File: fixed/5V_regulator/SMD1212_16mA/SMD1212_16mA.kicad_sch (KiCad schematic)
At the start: 14 parts, among them J1 Conn_01x04, J2 Conn_01x04, Q1 MMBT5551L, U1 TPS61222DCK, U2 LMV321

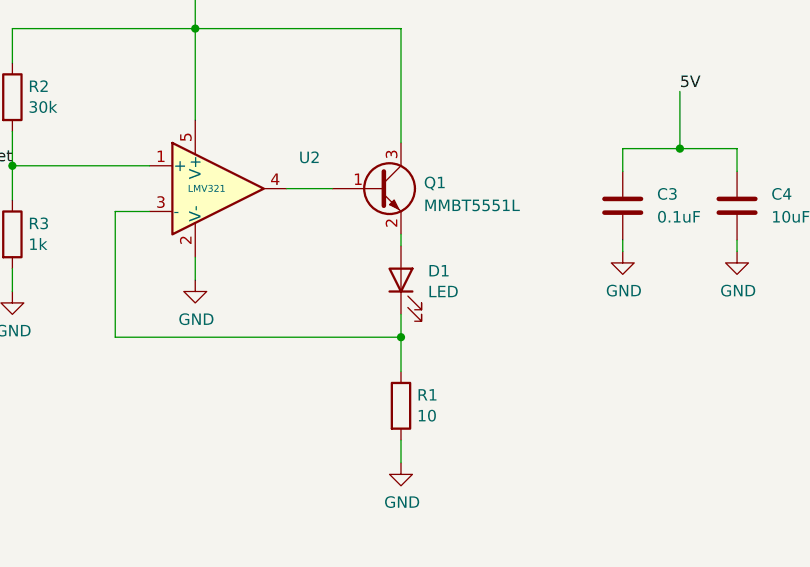
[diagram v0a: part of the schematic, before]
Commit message: Added part # to 'Symbol Fields Table" for SMD1212_16mA design.
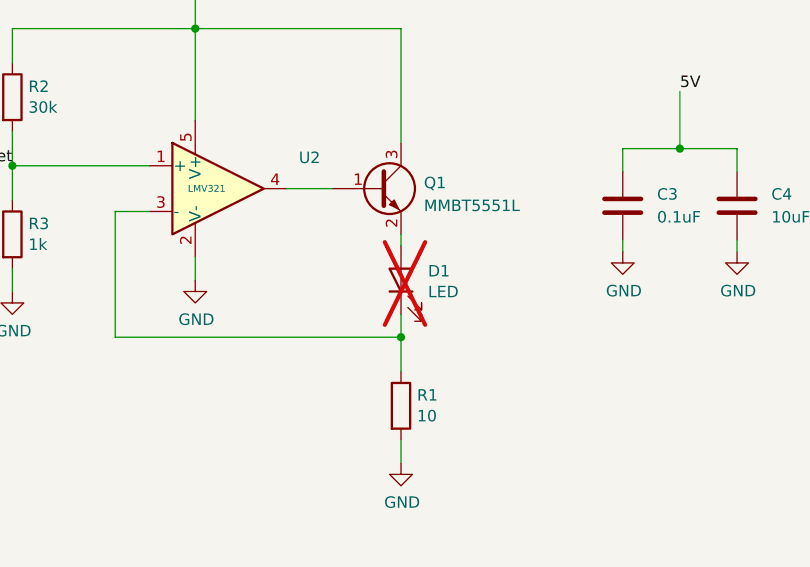
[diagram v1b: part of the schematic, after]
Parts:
- C1, C2, C4: LCSC Part # (none) -> C315248
- C3: LCSC Part # (none) -> C1525
- D1: now not fitted; now left out of the parts list
- J1, J2: LCSC Part # (none) -> C160404
- L1: LCSC Part # (none) -> C114862
- Q1: LCSC Part # (none) -> C41095
- R1: LCSC Part # (none) -> C413044
- R2: LCSC Part # (none) -> C138008
- R3: LCSC Part # (none) -> C144789
- U1: LCSC Part # (none) -> C116461
- U2: LCSC Part # (none) -> C7972
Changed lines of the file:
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@@
+			)
+		)
+		(property "LCSC Part #" "C160404"
+			(at 222.758 35.433 0)
+			(effects
+				(font
+					(size 1.27 1.27)
+				)
+				(hide yes)
 			)
 		)
@@
 			)
 		)
+		(property "LCSC Part #" "C160404"
+			(at 258.953 35.433 0)
+			(effects
+				(font
+					(size 1.27 1.27)
+				)
+				(hide yes)
+			)
+		)
 		(pin "1"
 		)
@@
 		(unit 1)
 		(exclude_from_sim no)
-		(in_bom yes)
-		(on_board yes)
-		(dnp no)
+		(in_bom no)
+		(on_board yes)
+		(dnp yes)
 		(property "Reference" "D1"
 			(at 160.3502 62.8904 90)
@@
 					(size 1.27 1.27)
 				)
+			)
+		)
+		(property "LCSC Part #" "C413044"
+			(at 157.353 77.851 0)
+			(effects
+				(font
+					(size 1.27 1.27)
+				)
+				(hide yes)
 			)
 		)
@@
 			)
 		)
+		(property "LCSC Part #" "C315248"
+			(at 194.691 55.626 0)
+			(effects
+				(font
+					(size 1.27 1.27)
+				)
+				(hide yes)
+			)
+		)
 		(pin "1"
 		)
@@
 					(size 1.27 1.27)
 				)
+			)
+		)
+		(property "LCSC Part #" "C1525"
+			(at 181.991 55.626 0)
+			(effects
+				(font
+					(size 1.27 1.27)
+				)
+				(hide yes)
 			)
 		)
@@
 			)
 		)
+		(property "LCSC Part #" "C116461"
+			(at 56.896 40.64 0)
+			(effects
+				(font
+					(size 1.27 1.27)
+				)
+				(hide yes)
+			)
+		)
 		(pin "1"
 		)
@@
 			)
 		)
+		(property "LCSC Part #" "C315248"
+			(at 32.131 46.736 0)
+			(effects
+				(font
+					(size 1.27 1.27)
+				)
+				(hide yes)
+			)
+		)
 		(pin "1"
 		)
@@
 			)
 		)
+		(property "LCSC Part #" "C315248"
+			(at 76.962 44.196 0)
+			(effects
+				(font
+					(size 1.27 1.27)
+				)
+				(hide yes)
+			)
+		)
 		(pin "1"
 		)
@@
 			)
 		)
+		(property "LCSC Part #" "C138008"
+			(at 114.173 43.561 0)
+			(effects
+				(font
+					(size 1.27 1.27)
+				)
+				(hide yes)
+			)
+		)
 		(pin "1"
 		)
@@
 					(size 1.27 1.27)
 				)
+			)
+		)
+		(property "LCSC Part #" "C7972"
+			(at 137.033 53.721 0)
+			(effects
+				(font
+					(size 1.27 1.27)
+				)
+				(hide yes)
 			)
 		)
@@
 			)
 		)
+		(property "LCSC Part #" "C41095"
+			(at 154.813 53.721 0)
+			(effects
+				(font
+					(size 1.27 1.27)
+				)
+				(hide yes)
+			)
+		)
 		(pin "1"
 		)
@@
 					(size 1.27 1.27)
 				)
+			)
+		)
+		(property "LCSC Part #" "C144789"
+			(at 114.173 58.801 0)
+			(effects
+				(font
+					(size 1.27 1.27)
+				)
+				(hide yes)
 			)
 		)
@@
 			)
 		)
+		(property "LCSC Part #" "C114862"
+			(at 40.513 38.1 90)
+			(effects
+				(font
+					(size 1.27 1.27)
+				)
+				(hide yes)
+			)
+		)
